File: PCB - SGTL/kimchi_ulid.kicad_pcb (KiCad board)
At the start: 4 copper layers, 65 x 45.4 mm, 43 parts, among them J1 RCJ-2123, J2 DF40HC(3.5)-60DS, J3 DF40HC(3.5)-60DS, J4 RCJ-2123, J5 54-00176, U1 24C32, U2 SGTL5000XNLA3

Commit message: SGTL Version
 SGTL version finished, need feedback, chip is weird the route is too
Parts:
- moved C18 19.0 mm to (147.9, 95.8), turned to 180 degrees
- moved C19 14.9 mm to (147.4, 94.0), turned to 180 degrees
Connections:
- U2 pad 16: Net-(U2-Pad16) -> SAI3_RXD
- U2 pad 18: SAI3_RXD -> I2C3_SDA
- U2 pad 19: SAI3_RXFS -> I2C3_SCL
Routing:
- net I2C3_SCL: track 1.40 -> 20.8 mm, vias 1 -> 3
- net I2C3_SDA: track 1.20 -> 18.8 mm, vias 1 -> 3
- net SAI3_RXFS: track 16.3 -> 1.32 mm
- net MIC_BIAS: track 33.3 -> 35.2 mm
- net GND: track 59.9 -> 61.8 mm, vias 70 -> 72
- net MIC_IN: track 31.9 -> 30.1 mm
- net SAI3_RXD: track 16.3 -> 17.3 mm, vias 1 -> 3

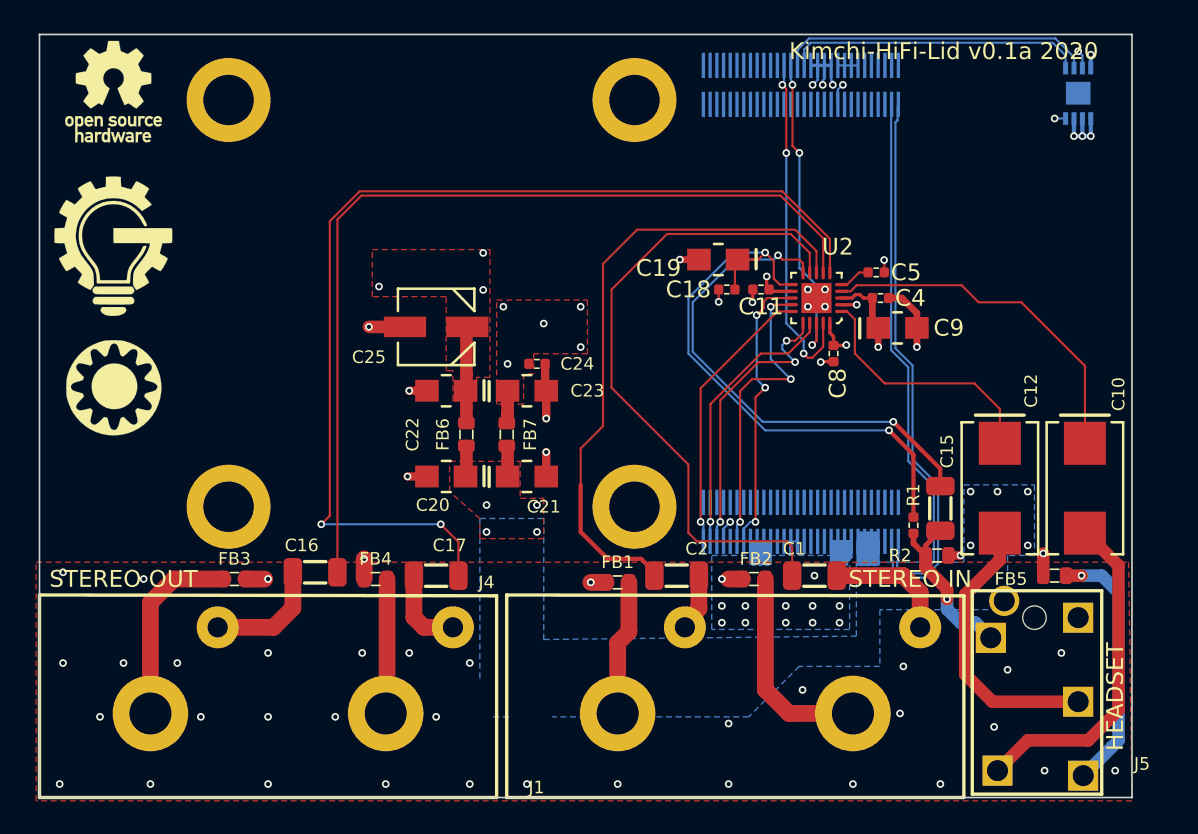
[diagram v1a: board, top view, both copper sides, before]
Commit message: Test Points
Test points added, also traces cleaned up and widened in places where more current capacity is required or appreciated.
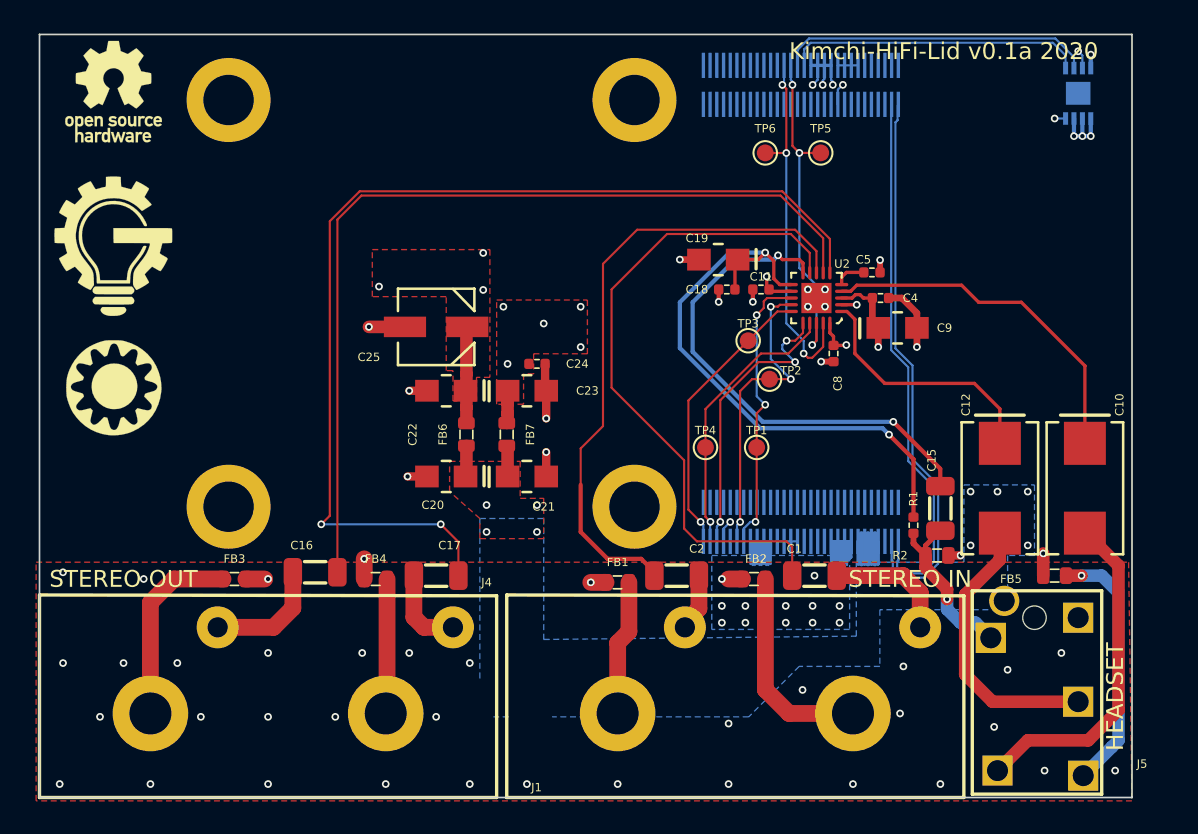
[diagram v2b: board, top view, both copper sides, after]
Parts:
- added TP1: TestPoint, kimchi_ulid:TestPoint_Pad_D1.0mm, F.Cu at (149.7, 105.2)
- added TP2: TestPoint, kimchi_ulid:TestPoint_Pad_D1.0mm, F.Cu at (150.4, 101.1)
- added TP3: TestPoint, kimchi_ulid:TestPoint_Pad_D1.0mm, F.Cu at (149.2, 98.8)
- added TP4: TestPoint, kimchi_ulid:TestPoint_Pad_D1.0mm, F.Cu at (146.6, 105.2)
- added TP5: TestPoint, kimchi_ulid:TestPoint_Pad_D1.0mm, F.Cu at (153.5, 87.6)
- added TP6: TestPoint, kimchi_ulid:TestPoint_Pad_D1.0mm, F.Cu at (150.2, 87.6)
- moved C5 0.25 mm to (156.5, 94.8)
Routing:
- net I2C3_SDA: track 18.8 -> 20.0 mm
- net I2C3_SCL: track 20.8 -> 22.1 mm
- net SAI3_TXC: track 16.5 -> 17.1 mm
- net MIC_BIAS: track 35.2 -> 35.7 mm

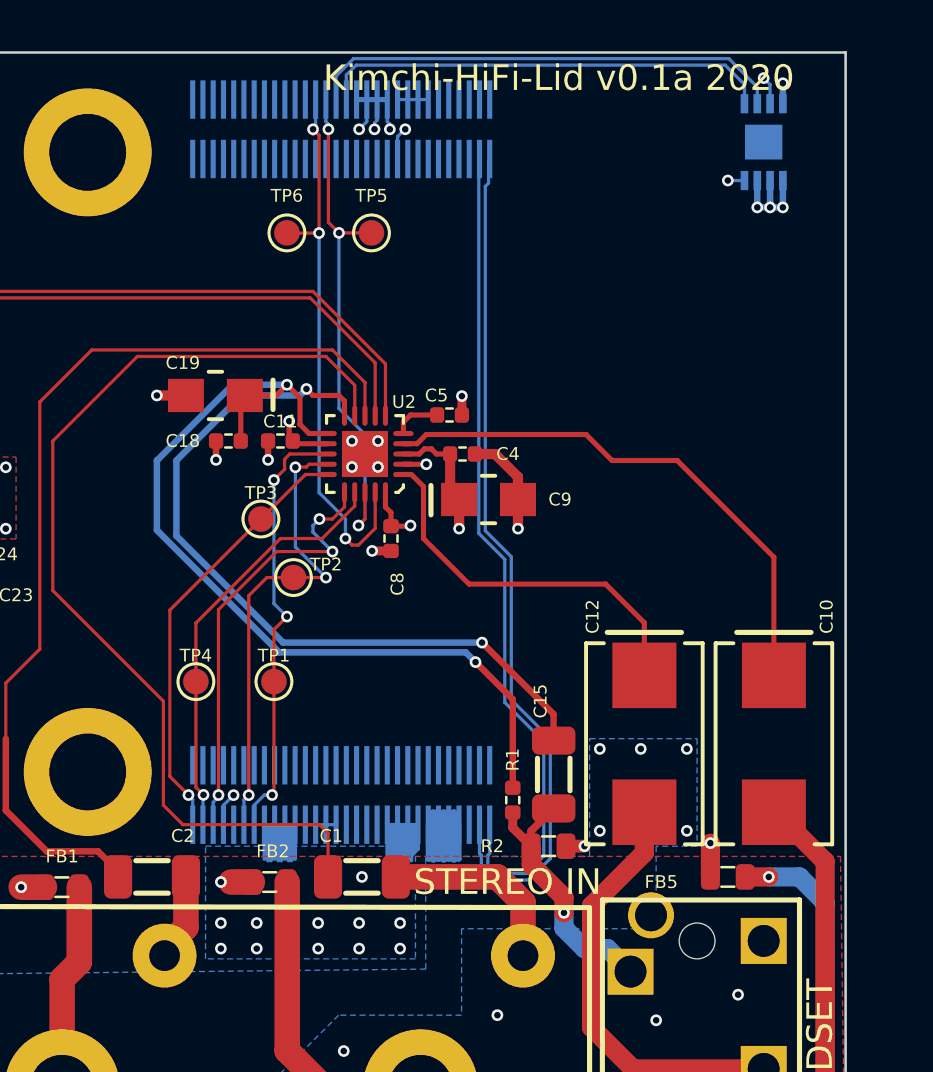
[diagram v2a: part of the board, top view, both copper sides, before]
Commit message: Headphone Detect and DRC
Cleared DRC violations, added and implemented a headphone detect circuit.
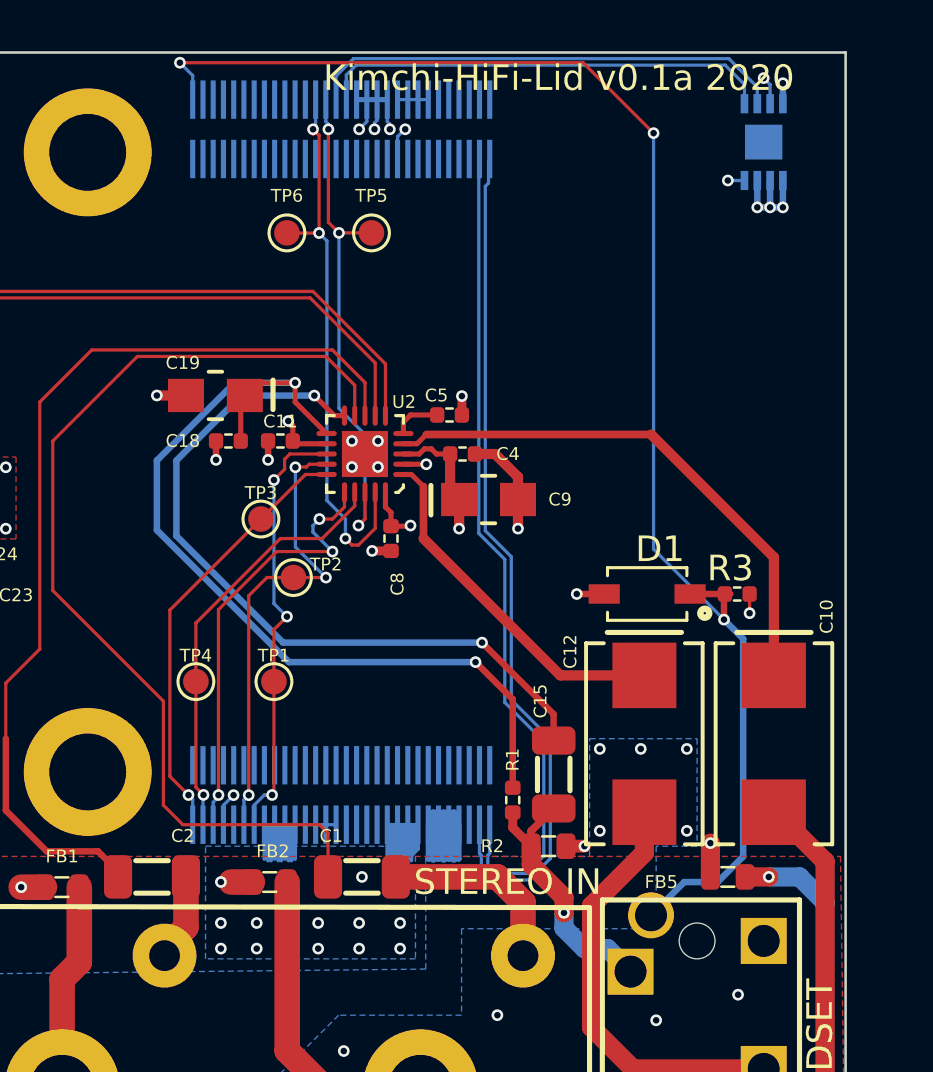
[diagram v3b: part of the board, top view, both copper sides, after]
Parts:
- added D1: MMSZ4688T3G, kimchi_ulid:MMSZ4688T3G, F.Cu at (164.2, 101.8)
- added R3: AC0402FR-071ML, kimchi_ulid:R0402, F.Cu at (167.8, 101.8)
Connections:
- J5 pad 5: Net-(J5-Pad5) -> ECSPI2_MISO
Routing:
- net ECSPI2_MISO: track 0.00 -> 58.1 mm, vias 0 -> 3
- net Net-(C12-Pad1): track 16.3 -> 15.1 mm
- net GND: track 61.7 -> 62.8 mm, vias 72 -> 73
- net VDD_3V3: track 20.5 -> 21.3 mm, vias 13 -> 14
- net MIC_IN: track 30.1 -> 29.5 mm

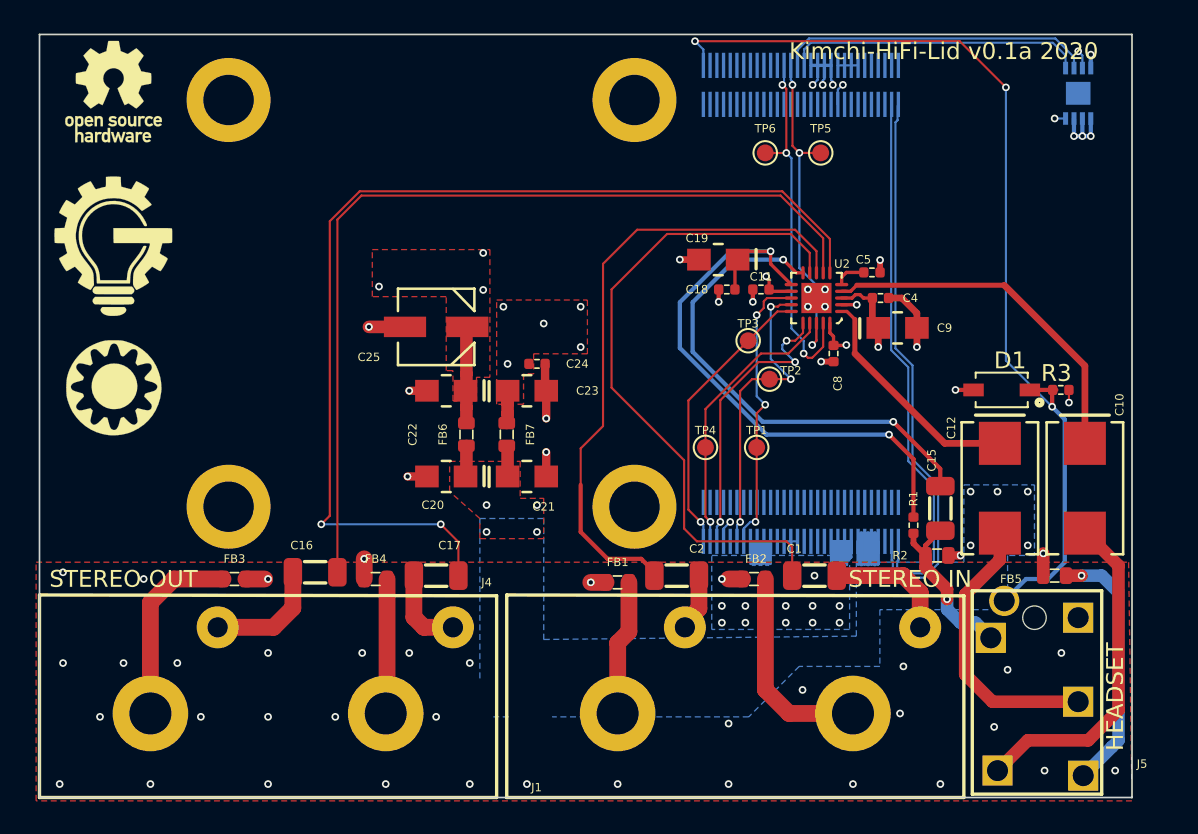
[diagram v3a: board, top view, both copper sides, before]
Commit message: Channel Swap
Swapped right and left channels on input, they were backwards. Changed soldermask rules so fab can make their own.
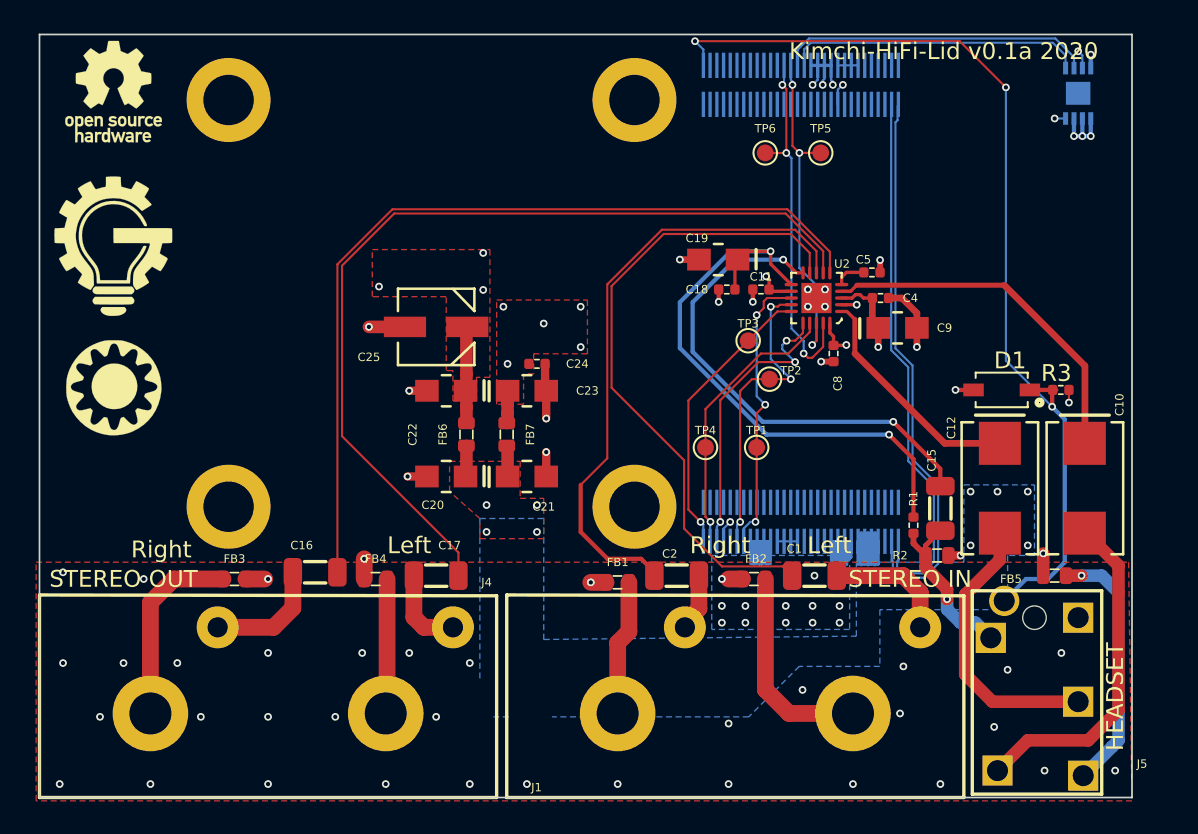
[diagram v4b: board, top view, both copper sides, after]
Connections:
- U2 pad 6: Net-(C17-Pad1) -> Net-(C16-Pad1)
- U2 pad 7: Net-(C16-Pad1) -> Net-(C17-Pad1)
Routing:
- net Net-(C17-Pad1): track 63.0 -> 53.9 mm, vias 2 -> 0
- net Net-(C16-Pad1): track 53.6 -> 51.3 mm
- net Net-(C1-Pad1): track 39.8 -> 38.9 mm
- net Net-(C2-Pad1): track 37.4 -> 36.6 mm
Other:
- rule pad_to_mask_clearance: 0.0508 -> 0
- board text added: "Left"
- board text added: "Right"
